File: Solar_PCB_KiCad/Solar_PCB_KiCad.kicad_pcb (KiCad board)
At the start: 2 copper layers, 16 parts, among them J1 Screw_Terminal_01x02, J2 Screw_Terminal_01x02, U1 LT3652EMSE

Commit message: Updated PCB
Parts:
- added C3: 10u, Capacitor_SMD:C_0603_1608Metric, F.Cu at (154.0, 91.5)
- added C4: 1u, Capacitor_SMD:C_0603_1608Metric, F.Cu at (154.0, 94.0)
- added D5: D_Schottky, Diode_SMD:D_SOD-323, F.Cu at (161.4, 117.2)
- added J3: Screw_Terminal_01x02, TerminalBlock_Phoenix:TerminalBlock_Phoenix_MKDS-1,5-2-5.08_1x02_P5.08mm_Horizontal, F.Cu at (143.3, 115.2)
- added R7: 270k, Resistor_SMD:R_0603_1608Metric, F.Cu at (162.0, 91.5)
- added R8: 100k, Resistor_SMD:R_0603_1608Metric, F.Cu at (162.0, 94.0)
- C1: value C -> 10u
- C2: value C -> 1u
- D1: value LED -> GREEN LED
- D2: value LED -> RED LED
- D3: footprint Diode_SMD:D_0603_1608Metric -> Diode_SMD:D_SOD-323
- D4: footprint Diode_SMD:D_0603_1608Metric -> Diode_SMD:D_SMC
- L1: value L -> 20uH; footprint Inductor_SMD:L_0603_1608Metric -> Inductor_THT:L_Radial_D7.8mm_P5.00mm_Fastron_07HCP
- R1, R2: value R -> 1.1k
- R3: value R -> 68k
- R4: value R -> 330k
- R5: value R -> 410k
- R6: value R -> 0.2
- moved D3 24.6 mm to (161.4, 114.3)
- moved D2 20.7 mm to (163.8, 106.9)
- moved D1 20.7 mm to (163.8, 104.3)
- moved U1 19.0 mm to (155.6, 115.8)
- moved R5 18.5 mm to (162.0, 86.5)
- moved R6 18.5 mm to (162.0, 89.0)
- moved L1 18.1 mm to (154.3, 107.9)
- moved R1 7.97 mm to (158.0, 86.5)
- moved R2 7.97 mm to (158.0, 89.0)
- moved R4 7.97 mm to (158.0, 94.0)
- moved R3 7.97 mm to (158.0, 91.5)
- moved D4 6.53 mm to (157.4, 99.2)
- moved C1 2.12 mm to (154.0, 86.5)
- moved C2 2.12 mm to (154.0, 89.0)
- moved J1 2.12 mm to (143.3, 91.5)
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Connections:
- D2 pad 2: Net-(D2-A) -> Net-(D1-A)
- J1 pad 1: Net-(J1-Pin_1) -> Net-(D5-A)
- J2 pad 2: unconnected-(J2-Pin_2-Pad2) -> GND
- R1 pad 1: Net-(J1-Pin_1) -> Net-(D1-K)
- R1 pad 2: Net-(D1-A) -> Net-(U1-~{CHRG})
- R2 pad 1: Net-(J1-Pin_1) -> Net-(D2-K)
- R2 pad 2: Net-(D2-A) -> Net-(U1-~{FAULT})
- U1 pad 1: Net-(J1-Pin_1) -> Net-(D1-A)
- U1 pad 2: Net-(J1-Pin_1) -> Net-(U1-V_{IN_REG})
- U1 pad 3: Net-(J1-Pin_1) -> Net-(D1-A)
- U1 pad 4: Net-(D1-K) -> Net-(U1-~{CHRG})
- U1 pad 5: Net-(D2-K) -> Net-(U1-~{FAULT})

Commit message: Updated PCB Layout
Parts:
- moved C1 34.1 mm to (157.2, 120.4), turned to -90 degrees
- moved R5 33.9 mm to (154.7, 119.6), turned to 180 degrees
- moved R1 33.1 mm to (142.2, 115.6)
- moved R2 32.8 mm to (143.0, 118.2), turned to 90 degrees
- moved J2 32.5 mm to (170.7, 120.9), turned to 90 degrees
- moved J3 28.2 mm to (170.7, 108.5), turned to 90 degrees
- moved R8 28.0 mm to (141.3, 112.9)
- moved R3 27.8 mm to (152.1, 118.7), turned to -90 degrees
- moved R7 27.5 mm to (144.7, 112.9)
- moved D1 27.2 mm to (139.9, 117.3), turned to 180 degrees
- moved R4 27.0 mm to (149.5, 119.6)
- moved D2 26.9 mm to (139.9, 119.4), turned to 180 degrees
- moved R6 25.9 mm to (162.3, 114.9), turned to -90 degrees
- moved C2 25.1 mm to (152.1, 114.1), turned to -90 degrees
- moved D5 21.6 mm to (141.2, 109.7), turned to 180 degrees
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
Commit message: Updated PCB Layout
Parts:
- D4: footprint Diode_SMD:D_SMC -> Diode_SMD:D_SOD-323
- moved C1 19.6 mm to (158.4, 100.9), turned to 90 degrees
- moved R6 12.4 mm to (157.7, 103.3), turned to 180 degrees
- moved C4 5.89 mm to (146.3, 111.2), turned to 0 degrees
- moved L1 5.46 mm to (151.9, 108.3), turned to 90 degrees
- moved D4 4.55 mm to (149.5, 111.4), turned to 180 degrees
- moved C3 3.88 mm to (146.3, 112.8), turned to 0 degrees
- moved R1 3.46 mm to (142.3, 119.0), turned to 90 degrees
- moved J2 3.14 mm to (167.7, 122.0)
- moved J3 3.14 mm to (167.7, 109.5)
- moved R7 2.10 mm to (143.0, 114.2)
- moved D5 2.05 mm to (142.7, 111.2)
- moved D1 1.88 mm to (140.7, 119.1), turned to 90 degrees
- moved R8 1.81 mm to (140.0, 114.2)
- moved R2 1.17 mm to (143.8, 119.0)
- moved D2 0.84 mm to (139.2, 119.1), turned to 90 degrees
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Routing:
- net Net-(D1-A): track 0.00 -> 9.93 mm
- net Net-(D2-K): track 0.00 -> 6.96 mm
- net Net-(U1-~{CHRG}): track 0.00 -> 4.74 mm
- net Net-(U1-~{FAULT}): track 0.00 -> 2.66 mm
- net Net-(D1-K): track 0.00 -> 1.55 mm
- added copper zone on F.Cu, net Net-(D1-A)

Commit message: Updated PCB Layout
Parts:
- D4: footprint Diode_SMD:D_SOD-323 -> Diode_SMD:D_SMC_Handsoldering
- L1: value 20uH -> 24uH; footprint Inductor_THT:L_Radial_D7.8mm_P5.00mm_Fastron_07HCP -> Inductor_SMD:L_Wuerth_WE-PDF_Handsoldering
- moved R6 16.4 mm to (172.6, 110.2)
- moved C1 16.4 mm to (173.5, 107.5)
- moved J2 15.5 mm to (183.2, 122.2)
- moved J3 15.4 mm to (183.2, 110.1)
- moved L1 11.3 mm to (163.0, 110.2), turned to 0 degrees
- moved D4 6.31 mm to (151.8, 105.5), turned to 90 degrees
- moved C2 0.37 mm to (151.7, 114.0)
- moved D3 0.36 mm to (154.2, 114.5)
- moved R3 0.14 mm to (152.1, 118.5)
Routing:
- net Net-(D3-A): track 0.00 -> 36.2 mm
- net Net-(U1-SENSE): track 0.00 -> 30.3 mm, vias 0 -> 2
- net Net-(D5-A): track 0.00 -> 9.92 mm
- net Net-(U1-V_{IN_REG}): track 0.00 -> 4.28 mm
- net Net-(U1-V_{FB}): track 0.00 -> 2.23 mm
- added copper zone on F.Cu, net Net-(R3-Pad2)
- added copper zone on F.Cu, net Net-(U1-V_{IN_REG})

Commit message: Updated layout & render
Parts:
- added G***: LOGO, LOGO, F.Cu at (129.5, 122.0)
- moved J2 2.44 mm to (180.8, 121.7)
- moved J3 2.39 mm to (180.8, 110.2)
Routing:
- net Net-(D3-A): track 36.2 -> 63.7 mm
- net Net-(D1-A): track 9.93 -> 11.5 mm
- added copper zone on B.Cu, net GND
- added copper zone on F.Cu, net GND
- added copper zone on F.Cu, net Net-(D3-K)
- added copper zone on F.Cu, net Net-(D4-K)
- added copper zone on F.Cu, net Net-(U1-SENSE)
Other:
- board outline added: 70 x 39 mm
- board text added: "+"
- board text added: "Battery"
- board text added: "Load"
- board text added: "PCB3D_BR_Solar_PCB_KiCad"
- board text added: "PCB3D_TL_Solar_PCB_KiCad"
- board text added: "Solar Charger"
- board text added: "Solar Panel"

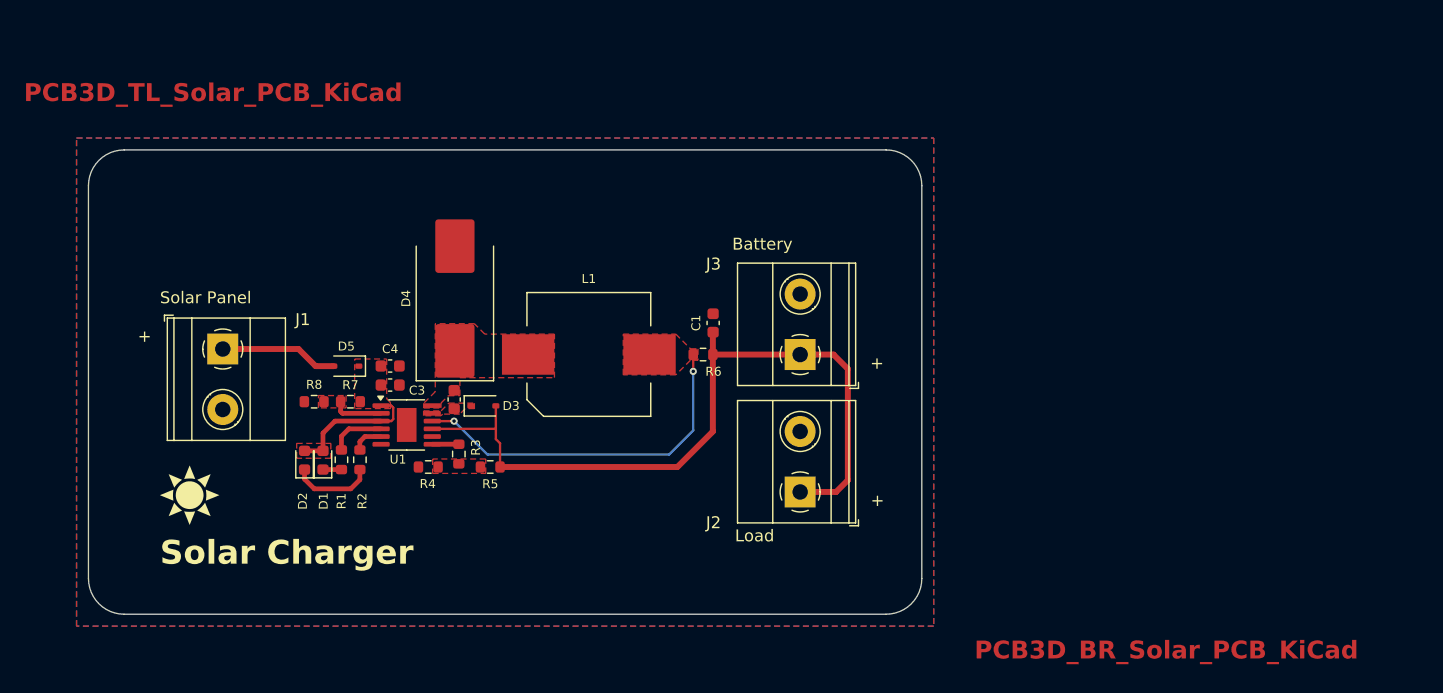
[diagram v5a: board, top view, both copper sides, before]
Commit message: Added grounded mounting holes
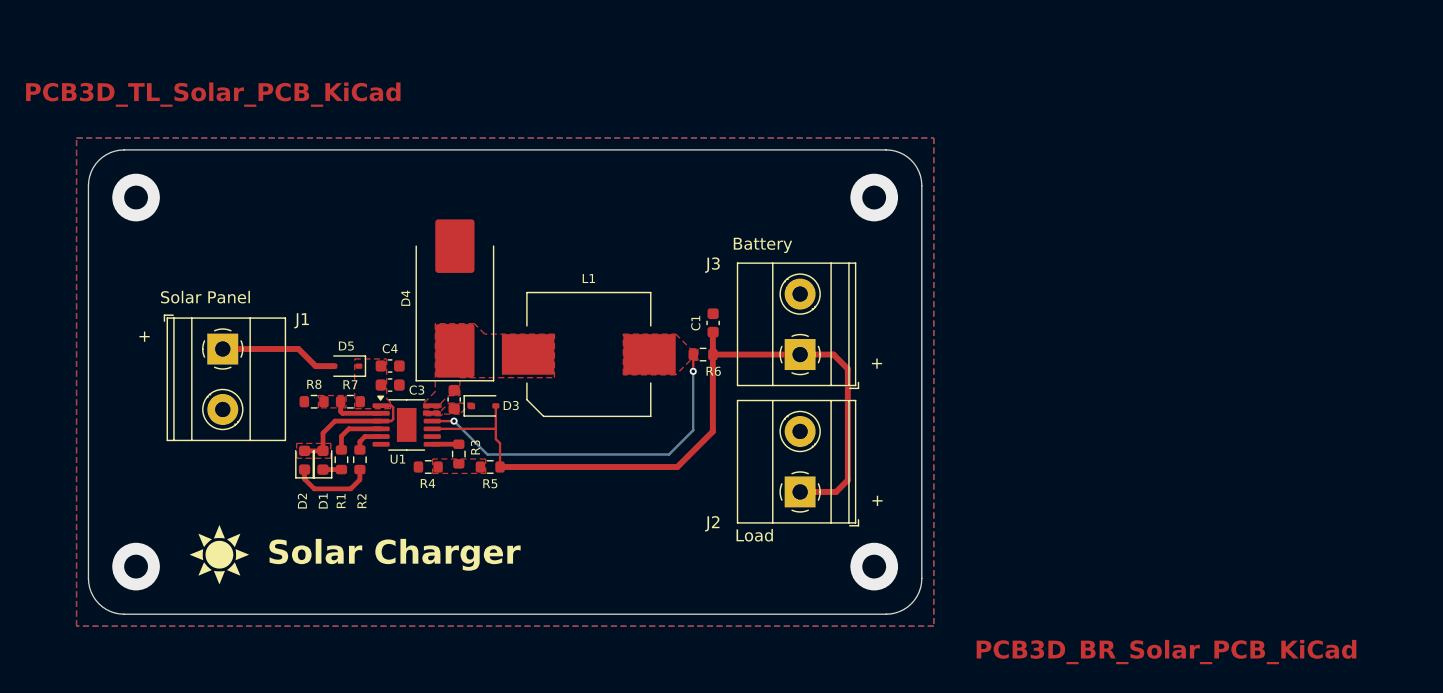
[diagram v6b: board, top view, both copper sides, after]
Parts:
- moved G*** 5.59 mm to (132.0, 127.0)
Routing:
- net GND: vias 0 -> 4
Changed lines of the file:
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@@
 			(svgprecision 4)
 			(plotframeref no)
-			(viasonmask no)
+			(viasonmask yes)
 			(mode 1)
 			(useauxorigin no)
@@
 	(footprint "LOGO"
 		(layer "F.Cu")
-		(at 129.5 122)
+		(at 132 127)
 		(property "Reference" "G***"
 			(at 0 0 0)
@@
 	)
 	(gr_text "Solar Charger"
-		(at 127 128 0)
+		(at 136 128 0)
 		(layer "F.SilkS")
 		(effects
@@
 		)
 	)
+	(via
+		(at 187 128)
+		(size 4)
+		(drill 2)
+		(layers "F.Cu" "B.Cu")
+		(free yes)
+		(net 1)
+	)
+	(via
+		(at 125 97)
+		(size 4)
+		(drill 2)
+		(layers "F.Cu" "B.Cu")
+		(free yes)
+		(net 1)
+	)
+	(via
+		(at 187 97)
+		(size 4)
+		(drill 2)
+		(layers "F.Cu" "B.Cu")
+		(free yes)
+		(net 1)
+	)
+	(via
+		(at 125 128)
+		(size 4)
+		(drill 2)
+		(layers "F.Cu" "B.Cu")
+		(free yes)
+		(net 1)
+	)
 	(segment

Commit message: Updated Layout
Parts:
- moved R4 3.85 mm to (151.9, 122.7), turned to 90 degrees
- moved R5 3.28 mm to (151.9, 118.0), turned to -90 degrees
- moved R3 2.31 mm to (150.7, 120.4), turned to 0 degrees
- moved D3 1.73 mm to (153.8, 116.2), turned to -90 degrees
- moved C2 1.13 mm to (152.5, 113.2), turned to 0 degrees
- moved G*** 1.00 mm to (132.0, 126.0)
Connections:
- J2 pad 1: Net-(D3-A) -> GND
- J2 pad 2: GND -> Net-(D3-A)
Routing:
- net Net-(D3-A): track 63.7 -> 32.7 mm
- net Net-(U1-SENSE): track 30.3 -> 28.9 mm
- net GND: vias 4 -> 144
- added copper zone on F.Cu, net Net-(D3-A)
